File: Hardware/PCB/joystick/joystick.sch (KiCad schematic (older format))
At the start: 36 parts, among them J1 Synth_power_2x5, J10 2_pin_Molex_header, J2 6 pin Molex header, J3 AudioJack2, J4 AudioJack2, J5 3_pin_Molex_connector, J8 2_pin_Molex_connector, J9 3_pin_Molex_header, U1 TL074

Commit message: Add gain trimmers and test points
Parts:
- added RV1: 20k, ao_tht:Potentiometer_Bourns_3296W_Vertical_screw_centered, symbol ao_symbols:R_POT_TRIM_3296W
- added TP1: X_gain, TestPoint:TestPoint_Pad_D2.0mm, symbol Connector:TestPoint
- C1, C2: footprint ao_tht:CP_Radial_D5.0mm_P2.00mm -> ao_tht:CP_Radial_D6.3mm_P2.50mm; symbol Device:CP -> ao_symbols:CP; Vendor (none) -> Tayda
- C3, C4: symbol Device:C -> ao_symbols:C; Vendor (none) -> Tayda
- D1, D2: symbol Device:D_Schottky -> ao_symbols:1N5817; SKU (none) -> A-159; Vendor (none) -> Tayda
- J1: Vendor (none) -> Tayda
- J4: renamed from J3; Vendor (none) -> Tayda
- J5: renamed from J2; Vendor (none) -> Tayda
- J6: renamed from J4; Vendor (none) -> Tayda
- R1: renamed from R4; symbol Device:R -> ao_symbols:R; Vendor (none) -> Tayda
- R10: renamed from R7; symbol Device:R -> ao_symbols:R; Vendor (none) -> Tayda
- R11: renamed from R8; symbol Device:R -> ao_symbols:R; Vendor (none) -> Tayda
- R12: renamed from R9; symbol Device:R -> ao_symbols:R; Vendor (none) -> Tayda
- R13: renamed from R10; symbol Device:R -> ao_symbols:R; Vendor (none) -> Tayda
- R14: renamed from R11; symbol Device:R -> ao_symbols:R; Vendor (none) -> Tayda
- R2: renamed from R12; value 20k -> 15k; symbol Device:R -> ao_symbols:R; Vendor (none) -> Tayda
- R3: renamed from R13; symbol Device:R -> ao_symbols:R; Vendor (none) -> Tayda
- R4: renamed from R14; symbol Device:R -> ao_symbols:R; Vendor (none) -> Tayda
- R5: renamed from R1; symbol Device:R -> ao_symbols:R; Vendor (none) -> Tayda
- R6: renamed from R2; value 20k -> 10k; symbol Device:R -> ao_symbols:R; Vendor (none) -> Tayda
- R7: renamed from R3; symbol Device:R -> ao_symbols:R; Vendor (none) -> Tayda
- R8: renamed from R5; symbol Device:R -> ao_symbols:R; Vendor (none) -> Tayda
- R9: renamed from R6; symbol Device:R -> ao_symbols:R; Vendor (none) -> Tayda
- RV2: renamed from RV1; symbol Device:R_POT -> ao_symbols:R_POT; Vendor (none) -> Tayda
- RV3: renamed from RV2; symbol Device:R_POT -> ao_symbols:R_POT; Vendor (none) -> Tayda
- U1: symbol Amplifier_Operational:TL074 -> ao_symbols:TL074; SKU (none) -> A-1138; Vendor (none) -> Tayda
- renumbered J5 to J2, J8 to J3, J9 to J7, J10 to J8
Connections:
- net at R7.2, U1.1: now also RV1.1, TP1.1; no longer R6.1
- new net: R6.1, RV1.2, RV1.3
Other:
- note added: "Adjust trimmer to \nget ±2.4 V at TP1"
- note added: "Check pot for reasonably\naccurate 100k from \npin 1 to 3 (within 10k)\n"
- moved on the sheet: R6

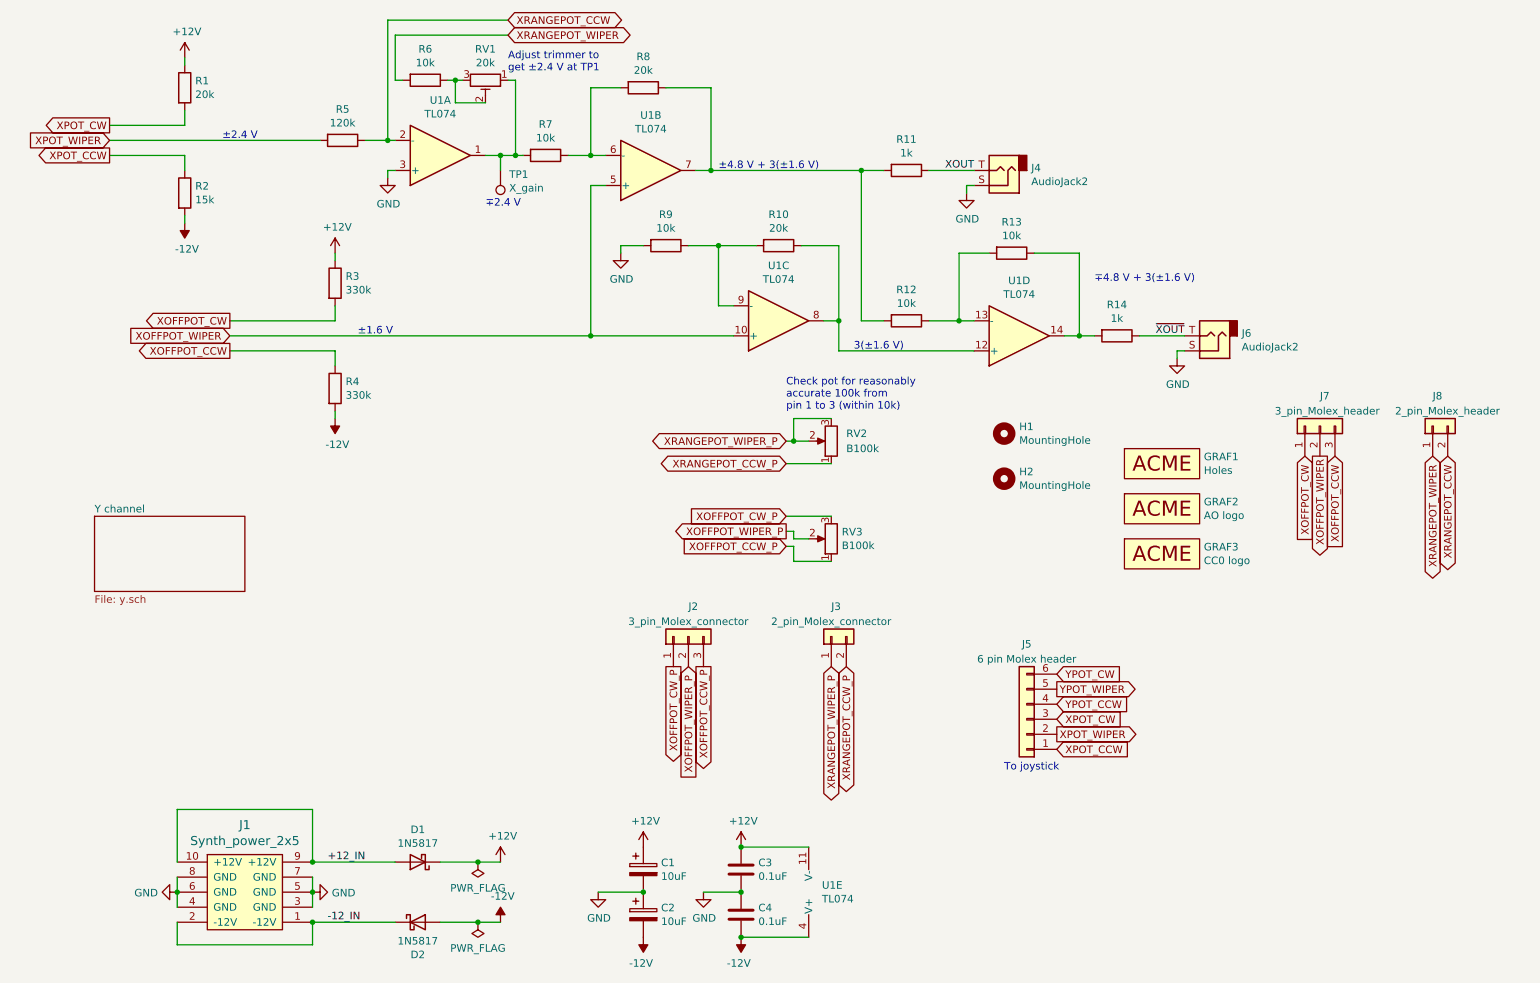
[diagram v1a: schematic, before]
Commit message: Move trimmers to inputs
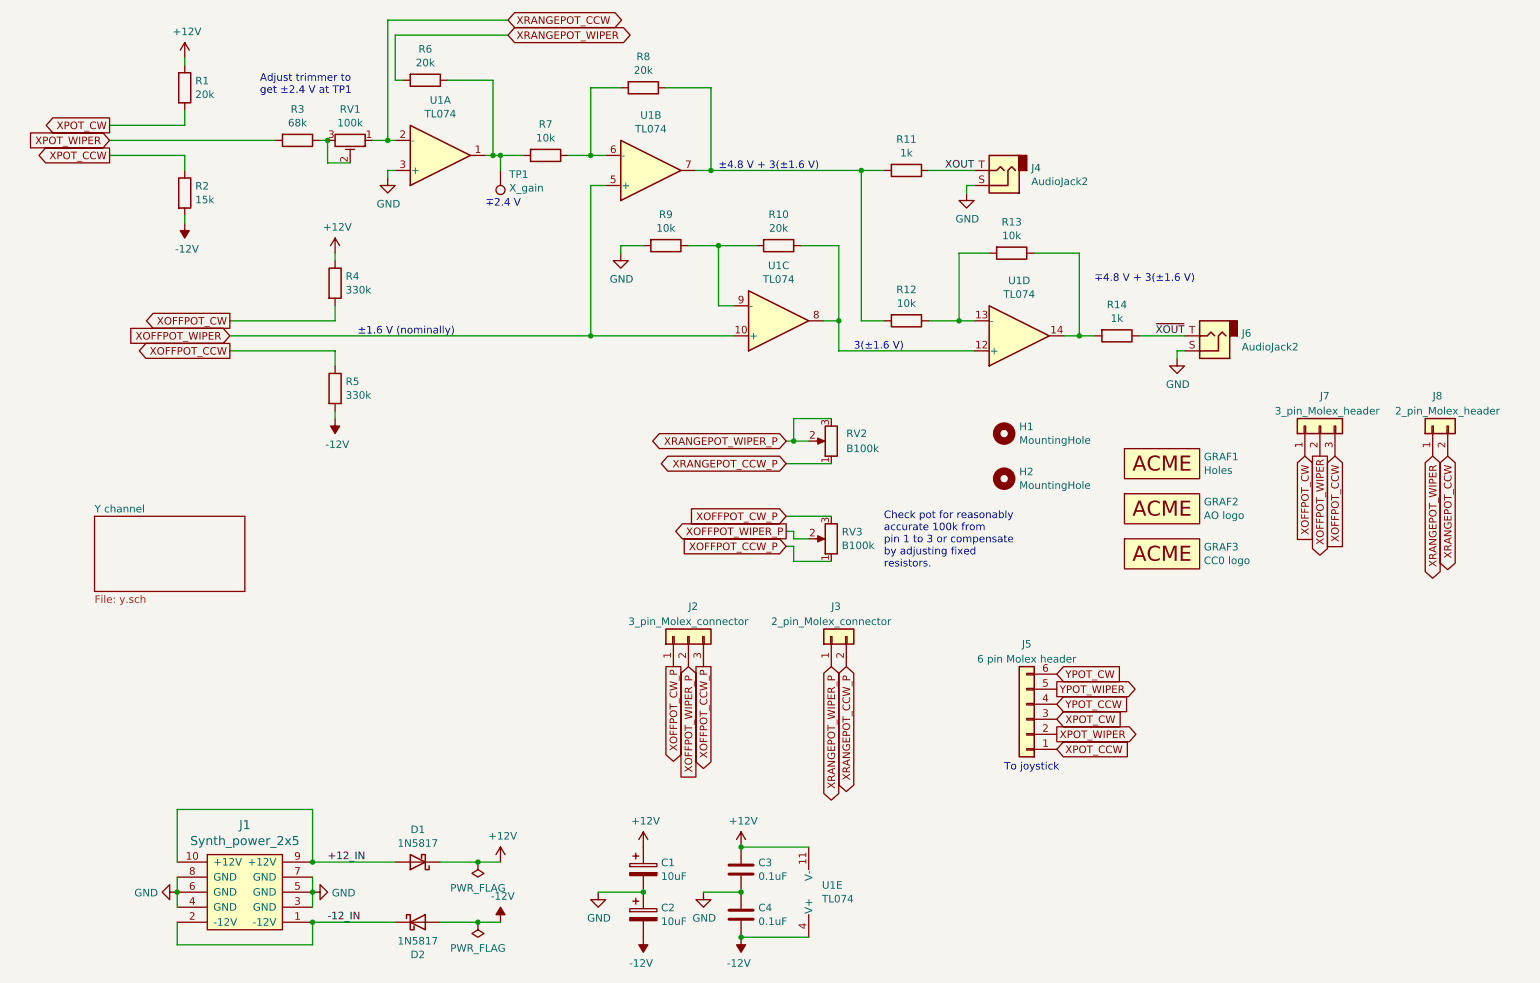
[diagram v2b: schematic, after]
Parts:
- R3: renamed from R5; value 120k -> 68k
- R6: value 10k -> 20k
- RV1: value 20k -> 100k
- renumbered R3 to R4, R4 to R5
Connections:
- net XRANGEPOT_CCW: now also RV1.1; no longer R3.1
- net at R7.2, TP1.1, U1.1: now also R6.1; no longer RV1.1
- net at RV1.2, RV1.3: now also R3.1; no longer R6.1
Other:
- note added: "Check pot for reasonably\naccurate 100k from \npin 1 to 3 or compensate\nby adjusting fixed\nresistors.\n"
- note added: "±1.6 V (nominally)"
- note removed: "Check pot for reasonably\naccurate 100k from \npin 1 to 3 (within 10k)\n"
- note removed: "±1.6 V"
- note removed: "±2.4 V"
- moved on the sheet: R3, RV1
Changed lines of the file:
@@
 $EndComp
 $Comp
-L ao_symbols:R R5
+L ao_symbols:R R3
 U 1 1 5FC19D49
-P 2650 2000
-F 0 "R5" V 2443 2000 50  0000 C CNN
-F 1 "120k" V 2534 2000 50  0000 C CNN
-F 2 "ao_tht:R_Axial_DIN0207_L6.3mm_D2.5mm_P10.16mm_Horizontal" V 2580 2000 50  0001 C CNN
-F 3 "~" H 2650 2000 50  0001 C CNN
-F 4 "Tayda" H 2650 2000 50  0001 C CNN "Vendor"
-	1    2650 2000
+P 2350 2000
+F 0 "R3" V 2143 2000 50  0000 C CNN
+F 1 "68k" V 2234 2000 50  0000 C CNN
+F 2 "ao_tht:R_Axial_DIN0207_L6.3mm_D2.5mm_P10.16mm_Horizontal" V 2280 2000 50  0001 C CNN
+F 3 "~" H 2350 2000 50  0001 C CNN
+F 4 "Tayda" H 2350 2000 50  0001 C CNN "Vendor"
+	1    2350 2000
 	0    1    1    0
 $EndComp
 Wire Wire Line
-	2800 2000 2950 2000
-Wire Wire Line
-	3800 1600 3800 2100
-Wire Wire Line
-	3800 2100 3700 2100
+	2500 2000 2550 2000
+Wire Wire Line
+	3650 1600 3650 2100
+Wire Wire Line
+	3650 2100 3700 2100
 Wire Wire Line
 	3050 1600 3000 1600
@@
 P 3200 1600
 F 0 "R6" V 2993 1600 50  0000 C CNN
-F 1 "10k" V 3084 1600 50  0000 C CNN
+F 1 "20k" V 3084 1600 50  0000 C CNN
 F 2 "ao_tht:R_Axial_DIN0207_L6.3mm_D2.5mm_P10.16mm_Horizontal" V 3130 1600 50  0001 C CNN
 F 3 "~" H 3200 1600 50  0001 C CNN
@@
 	0    1    1    0
 $EndComp
-Wire Wire Line
-	3350 1600 3400 1600
 Wire Wire Line
 	3000 1300 3000 1600
@@
 Wire Wire Line
 	2950 2200 2950 2250
-Connection ~ 3800 2100
+Connection ~ 3650 2100
 $Comp
 L power:+12V #PWR05
@@
 Connection ~ 5300 7300
 Wire Wire Line
-	1100 2000 2500 2000
-Wire Wire Line
-	3800 2100 3850 2100
+	1100 2000 2200 2000
 Wire Wire Line
 	4300 2300 4300 3300
@@
 ∓4.8 V + 3(±1.6 V)
 Text Notes 2750 3300 0    50   ~ 0
-±1.6 V
+±1.6 V (nominally)
 Text Notes 5150 2200 0    50   ~ 0
 ±4.8 V + 3(±1.6 V)
@@
 Wire Wire Line
 	1900 3300 4300 3300
-Text Notes 1850 2000 0    50   ~ 0
-±2.4 V
 Text Notes 3600 2450 0    50   ~ 0
 ∓2.4 V
@@
 	2600 3800 2600 3850
 $Comp
-L ao_symbols:R R3
+L ao_symbols:R R4
 U 1 1 609A7ECA
 P 2600 2950
-F 0 "R3" H 2670 2996 50  0000 L CNN
+F 0 "R4" H 2670 2996 50  0000 L CNN
 F 1 "330k" H 2670 2905 50  0000 L CNN
 F 2 "ao_tht:R_Axial_DIN0207_L6.3mm_D2.5mm_P10.16mm_Horizontal" V 2530 2950 50  0001 C CNN
@@
 $EndComp
 $Comp
-L ao_symbols:R R4
+L ao_symbols:R R5
 U 1 1 609A8185
 P 2600 3650
-F 0 "R4" H 2670 3696 50  0000 L CNN
+F 0 "R5" H 2670 3696 50  0000 L CNN
 F 1 "330k" H 2670 3605 50  0000 L CNN
 F 2 "ao_tht:R_Axial_DIN0207_L6.3mm_D2.5mm_P10.16mm_Horizontal" V 2530 3650 50  0001 C CNN
@@
 L ao_symbols:R_POT_TRIM_3296W RV1
 U 1 1 61838521
-P 3600 1600
-F 0 "RV1" V 3393 1600 50  0000 C CNN
-F 1 "20k" V 3484 1600 50  0000 C CNN
-F 2 "ao_tht:Potentiometer_Bourns_3296W_Vertical_screw_centered" H 3600 1600 50  0001 C CNN
-F 3 "~" H 3600 1600 50  0001 C CNN
-F 4 "Tayda" H 3600 1600 50  0001 C CNN "Vendor"
-F 5 "~" H 3600 1600 50  0001 C CNN "SKU"
-	1    3600 1600
+P 2700 2000
+F 0 "RV1" V 2493 2000 50  0000 C CNN
+F 1 "100k" V 2584 2000 50  0000 C CNN
+F 2 "ao_tht:Potentiometer_Bourns_3296W_Vertical_screw_centered" H 2700 2000 50  0001 C CNN
+F 3 "~" H 2700 2000 50  0001 C CNN
+F 4 "Tayda" H 2700 2000 50  0001 C CNN "Vendor"
+F 5 "~" H 2700 2000 50  0001 C CNN "SKU"
+	1    2700 2000
 	0    1    1    0
 $EndComp
-Wire Wire Line
-	3750 1600 3800 1600
-Wire Wire Line
-	3400 1600 3400 1750
-Wire Wire Line
-	3400 1750 3600 1750
-Connection ~ 3400 1600
-Wire Wire Line
-	3400 1600 3450 1600
-Text Notes 3750 1550 0    50   ~ 0
+Text Notes 2100 1700 0    50   ~ 0
 Adjust trimmer to \nget ±2.4 V at TP1
 $Comp
@@
 Connection ~ 3700 2100
 Wire Wire Line
-	3700 2100 3600 2100
-Text Notes 5600 3800 0    50   ~ 0
-Check pot for reasonably\naccurate 100k from \npin 1 to 3 (within 10k)\n
+	3650 2100 3600 2100
+Wire Wire Line
+	3700 2100 3850 2100
+Wire Wire Line
+	3350 1600 3650 1600
+Wire Wire Line
+	2850 2000 2950 2000
+Wire Wire Line
+	2550 2000 2550 2150
+Wire Wire Line
+	2550 2150 2700 2150
+Connection ~ 2550 2000
+Text Notes 6250 4850 0    50   ~ 0
+Check pot for reasonably\naccurate 100k from \npin 1 to 3 or compensate\nby adjusting fixed\nresistors.\n
 $EndSCHEMATC

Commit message: More tweaks, build.md
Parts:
- R4, R5: value 330k -> 300k
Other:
- note added: "±1.6 V (approx.,\ndepending on actual\npot value, PSU voltage,\nand Schottky diode\ndrop)"
- note removed: "±1.6 V (nominally)"
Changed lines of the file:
@@
 Text Notes 7650 2950 0    50   ~ 0
 ∓4.8 V + 3(±1.6 V)
-Text Notes 2750 3300 0    50   ~ 0
-±1.6 V (nominally)
 Text Notes 5150 2200 0    50   ~ 0
 ±4.8 V + 3(±1.6 V)
@@
 P 2600 2950
 F 0 "R4" H 2670 2996 50  0000 L CNN
-F 1 "330k" H 2670 2905 50  0000 L CNN
+F 1 "300k" H 2670 2905 50  0000 L CNN
 F 2 "ao_tht:R_Axial_DIN0207_L6.3mm_D2.5mm_P10.16mm_Horizontal" V 2530 2950 50  0001 C CNN
 F 3 "~" H 2600 2950 50  0001 C CNN
@@
 P 2600 3650
 F 0 "R5" H 2670 3696 50  0000 L CNN
-F 1 "330k" H 2670 3605 50  0000 L CNN
+F 1 "300k" H 2670 3605 50  0000 L CNN
 F 2 "ao_tht:R_Axial_DIN0207_L6.3mm_D2.5mm_P10.16mm_Horizontal" V 2530 3650 50  0001 C CNN
 F 3 "~" H 2600 3650 50  0001 C CNN
@@
 Text Notes 6250 4850 0    50   ~ 0
 Check pot for reasonably\naccurate 100k from \npin 1 to 3 or compensate\nby adjusting fixed\nresistors.\n
+Text Notes 3100 3750 0    50   ~ 0
+±1.6 V (approx.,\ndepending on actual\npot value, PSU voltage,\nand Schottky diode\ndrop)
 $EndSCHEMATC

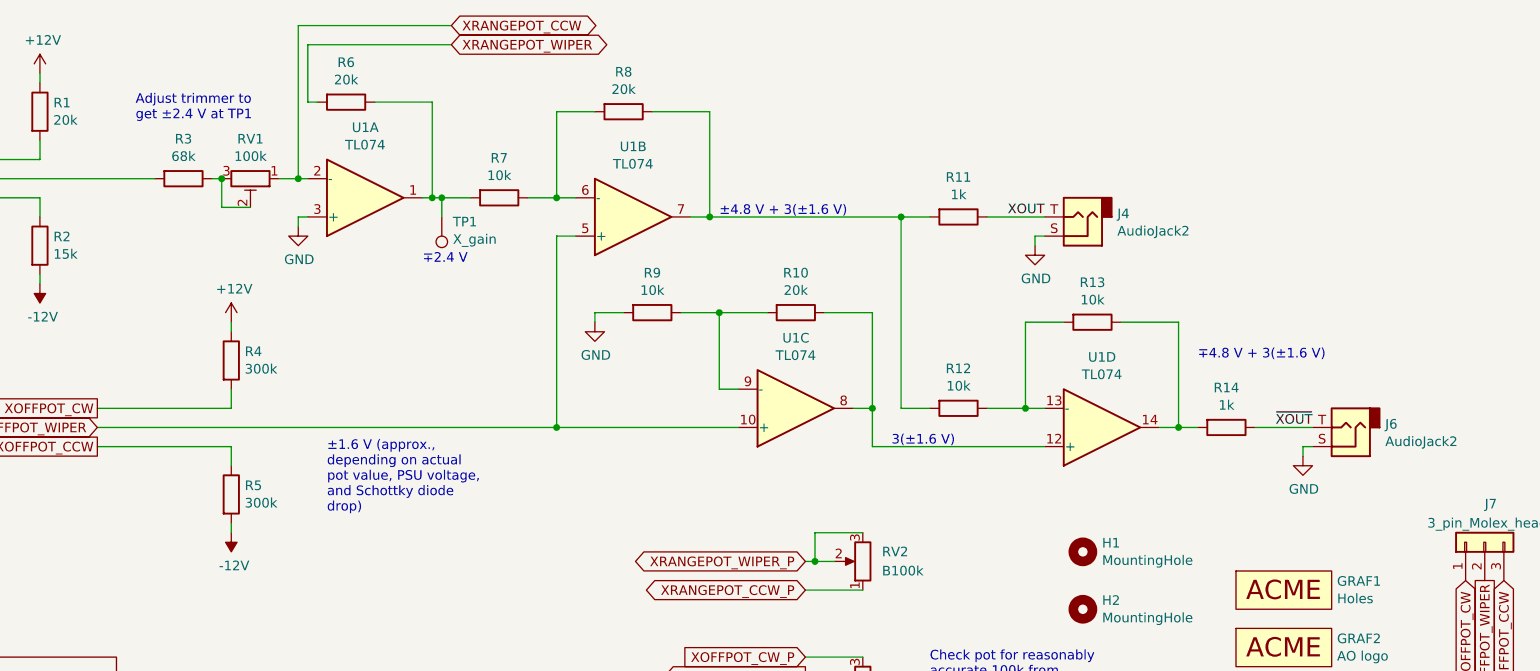
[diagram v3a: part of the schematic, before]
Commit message: Change voltage ranges
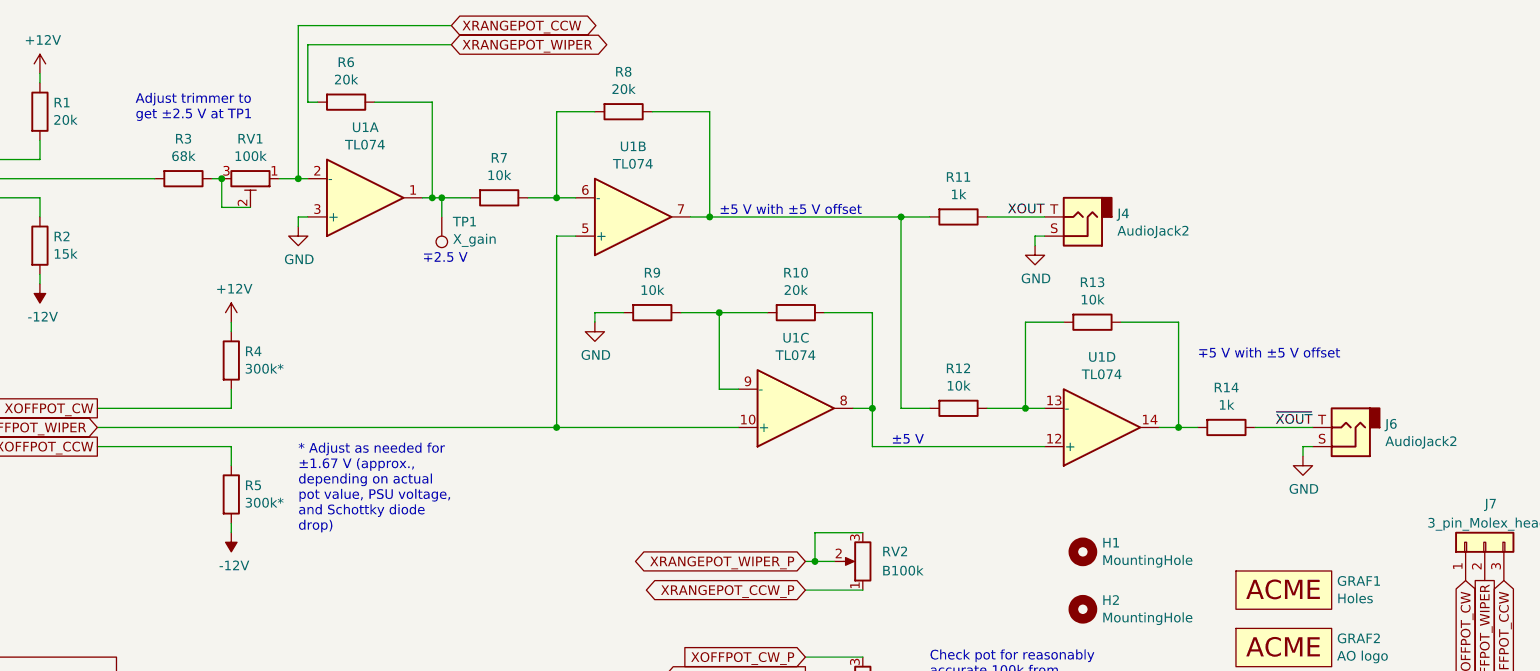
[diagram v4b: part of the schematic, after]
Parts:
- R4, R5: value 300k -> 300k*
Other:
- note added: "* Adjust as needed for\n±1.67 V (approx.,\ndepending on actual\npot value, PSU voltage,\nand Schottky diode\ndrop)"
- note added: "Adjust trimmer to \nget ±2.5 V at TP1"
- note added: "±5 V"
- note added: "±5 V with ±5 V offset"
- note added: "∓2.5 V"
- note added: "∓5 V with ±5 V offset"
- note removed: "3(±1.6 V)"
- note removed: "Adjust trimmer to \nget ±2.4 V at TP1"
- note removed: "±1.6 V (approx.,\ndepending on actual\npot value, PSU voltage,\nand Schottky diode\ndrop)"
- note removed: "±4.8 V + 3(±1.6 V)"
- note removed: "∓2.4 V"
- note removed: "∓4.8 V + 3(±1.6 V)"
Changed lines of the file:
@@
 $EndComp
 Text Notes 7650 2950 0    50   ~ 0
-∓4.8 V + 3(±1.6 V)
+∓5 V with ±5 V offset
 Text Notes 5150 2200 0    50   ~ 0
-±4.8 V + 3(±1.6 V)
+±5 V with ±5 V offset
 Text Notes 6050 3400 0    50   ~ 0
-3(±1.6 V)
+±5 V
 Wire Wire Line
 	1900 3300 4300 3300
 Text Notes 3600 2450 0    50   ~ 0
-∓2.4 V
+∓2.5 V
 $Comp
 L power:PWR_FLAG #FLG01
@@
 P 2600 2950
 F 0 "R4" H 2670 2996 50  0000 L CNN
-F 1 "300k" H 2670 2905 50  0000 L CNN
+F 1 "300k*" H 2670 2905 50  0000 L CNN
 F 2 "ao_tht:R_Axial_DIN0207_L6.3mm_D2.5mm_P10.16mm_Horizontal" V 2530 2950 50  0001 C CNN
 F 3 "~" H 2600 2950 50  0001 C CNN
@@
 P 2600 3650
 F 0 "R5" H 2670 3696 50  0000 L CNN
-F 1 "300k" H 2670 3605 50  0000 L CNN
+F 1 "300k*" H 2670 3605 50  0000 L CNN
 F 2 "ao_tht:R_Axial_DIN0207_L6.3mm_D2.5mm_P10.16mm_Horizontal" V 2530 3650 50  0001 C CNN
 F 3 "~" H 2600 3650 50  0001 C CNN
@@
 $EndComp
 Text Notes 2100 1700 0    50   ~ 0
-Adjust trimmer to \nget ±2.4 V at TP1
+Adjust trimmer to \nget ±2.5 V at TP1
 $Comp
 L Connector:TestPoint TP1
@@
 Text Notes 6250 4850 0    50   ~ 0
 Check pot for reasonably\naccurate 100k from \npin 1 to 3 or compensate\nby adjusting fixed\nresistors.\n
-Text Notes 3100 3750 0    50   ~ 0
-±1.6 V (approx.,\ndepending on actual\npot value, PSU voltage,\nand Schottky diode\ndrop)
+Text Notes 2950 3850 0    50   ~ 0
+* Adjust as needed for\n±1.67 V (approx.,\ndepending on actual\npot value, PSU voltage,\nand Schottky diode\ndrop)
 $EndSCHEMATC

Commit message: Move trimmers and TPs to back
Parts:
- RV1: footprint ao_tht:Potentiometer_Bourns_3296W_Vertical_screw_centered -> ao_tht:Potentiometer_Bourns_3296W_Vertical_standard
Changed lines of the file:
@@
 F 0 "RV1" V 2493 2000 50  0000 C CNN
 F 1 "100k" V 2584 2000 50  0000 C CNN
-F 2 "ao_tht:Potentiometer_Bourns_3296W_Vertical_screw_centered" H 2700 2000 50  0001 C CNN
+F 2 "ao_tht:Potentiometer_Bourns_3296W_Vertical_standard" H 2700 2000 50  0001 C CNN
 F 3 "~" H 2700 2000 50  0001 C CNN
 F 4 "Tayda" H 2700 2000 50  0001 C CNN "Vendor"

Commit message: Update docs, generate Gerbers
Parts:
- renumbered C2 to C1, C1 to C2, C4 to C3, C3 to C4, D2 to D1, D1 to D2
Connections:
- net +12V: now also C1.1, C3.1, D1.1 (K), U1.4 (V+); no longer C2.1, C4.1, D2.1 (K), U1.11 (V-)
- net +12_IN: now also D1.2 (A); no longer D2.2 (A)
- net -12V: now also C2.2, C4.2, D2.2 (A), U1.11 (V-); no longer C1.2, C3.2, D1.2 (A), U1.4 (V+)
- net -12_IN: now also D2.1 (K); no longer D1.1 (K)
- net GND: now also C1.2, C2.1, C3.2, C4.1; no longer C1.1, C2.2, C3.1, C4.2
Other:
- moved on the sheet: C1, C2, C3, C4, D1, D2
